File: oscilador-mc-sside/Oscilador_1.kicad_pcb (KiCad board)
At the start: 4 copper layers, 33 x 30 mm, 22 parts, among them J201 Conn_01x02, Q301 BC846, Q302 BC846, U201 40106

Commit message: Detalles de configuración.
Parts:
- moved MK101 1.41 mm to (203.5, 45.5)
- moved MK102 1.41 mm to (203.5, 67.5)
- moved MK103 1.41 mm to (228.5, 67.5)
- moved MK104 1.41 mm to (228.5, 45.5)
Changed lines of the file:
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@@
 		(0 "F.Cu" signal "1.F.Cu")
 		(1 "In1.Cu" power "2.In.Cu.GND")
-		(2 "In2.Cu" jumper "3.In.Cu.VCC")
+		(2 "In2.Cu" power "3.In.Cu.VCC")
 		(31 "B.Cu" signal "4.B.Cu")
 		(32 "B.Adhes" user "B.Adhesive")
@@
 	(footprint "MountingHole:MountingHole_2.2mm_M2"
 		(layer "F.Cu")
-		(at 204.5 46.5)
+		(at 203.5 45.5)
 		(descr "Mounting Hole 2.2mm, no annular, M2")
 		(tags "mounting hole 2.2mm no annular m2")
@@
 	(footprint "MountingHole:MountingHole_2.2mm_M2"
 		(layer "F.Cu")
-		(at 204.5 66.5)
+		(at 203.5 67.5)
 		(descr "Mounting Hole 2.2mm, no annular, M2")
 		(tags "mounting hole 2.2mm no annular m2")
@@
 	(footprint "MountingHole:MountingHole_2.2mm_M2"
 		(layer "F.Cu")
-		(at 229.5 66.5)
+		(at 228.5 67.5)
 		(descr "Mounting Hole 2.2mm, no annular, M2")
 		(tags "mounting hole 2.2mm no annular m2")
@@
 	(footprint "MountingHole:MountingHole_2.2mm_M2"
 		(layer "F.Cu")
-		(at 229.5 46.5)
+		(at 228.5 45.5)
 		(descr "Mounting Hole 2.2mm, no annular, M2")
 		(tags "mounting hole 2.2mm no annular m2")

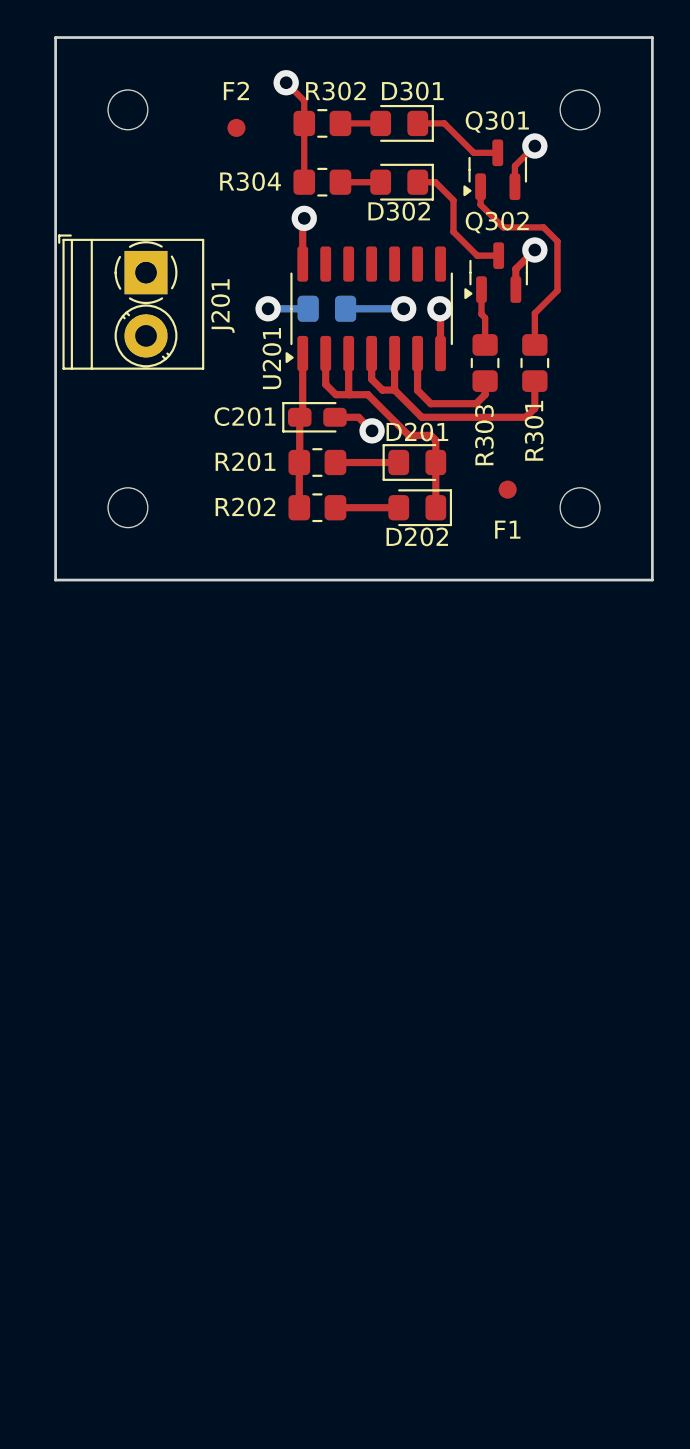
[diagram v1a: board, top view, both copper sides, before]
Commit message: Detalles de kicad multicapa 2024.
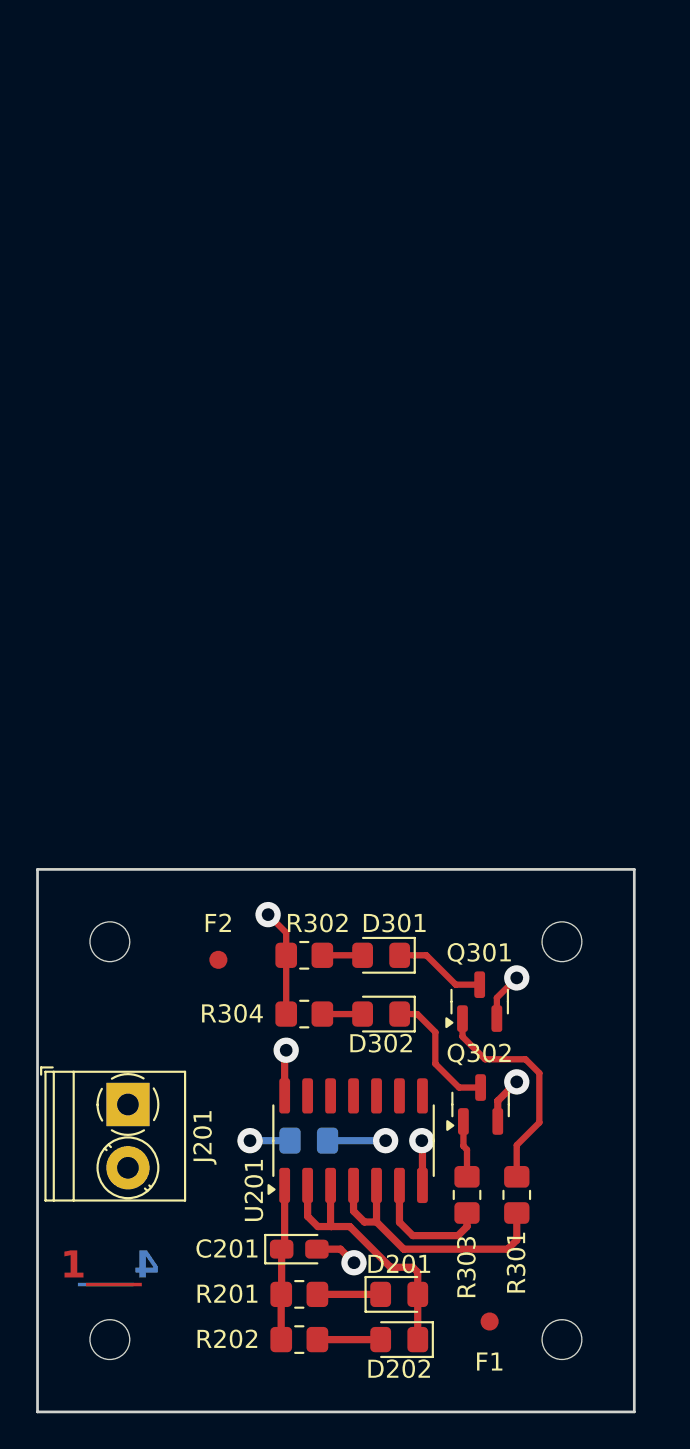
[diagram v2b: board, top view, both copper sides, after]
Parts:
- moved C201 46.0 mm to (213.0, 108.5)
- moved C202 46.0 mm to (213.5, 102.5)
- moved D201 46.0 mm to (218.5, 111.0)
- moved D202 46.0 mm to (218.5, 113.5)
- moved D301 46.0 mm to (217.5, 92.2)
- moved D302 46.0 mm to (217.5, 95.5)
- moved F1 46.0 mm to (223.5, 112.5)
- moved F2 46.0 mm to (208.5, 92.5)
- moved J201 46.0 mm to (203.5, 100.5)
- moved MK101 46.0 mm to (202.5, 91.5)
- moved MK102 46.0 mm to (202.5, 113.5)
- moved MK103 46.0 mm to (227.5, 113.5)
- moved MK104 46.0 mm to (227.5, 91.5)
- moved Q301 46.0 mm to (222.9, 94.8)
- moved Q302 46.0 mm to (223.0, 100.5)
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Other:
- rule pad_to_mask_clearance: 0.15 -> 0
- board text added: "1___"
- board text added: "4___"
- board text added: "_2__"
- board text added: "_3__"
